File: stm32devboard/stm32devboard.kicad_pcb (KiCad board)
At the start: 4 copper layers, 20.3 x 61 mm, 44 parts, among them J1 Conn_01x20, J2 Conn_01x20, J3 USB_C_Receptacle_USB2.0, J4 ARM_SWD_TagConnect_TC2030-NL, SW1 SW_SPST, SW2 SW_SPST, U1 STM32F042C6Tx, U2 AP63203WU, U3 TCAN332, U4 IP4234CZ6,125, X1 ECS-160-10-36Q-ES-TR

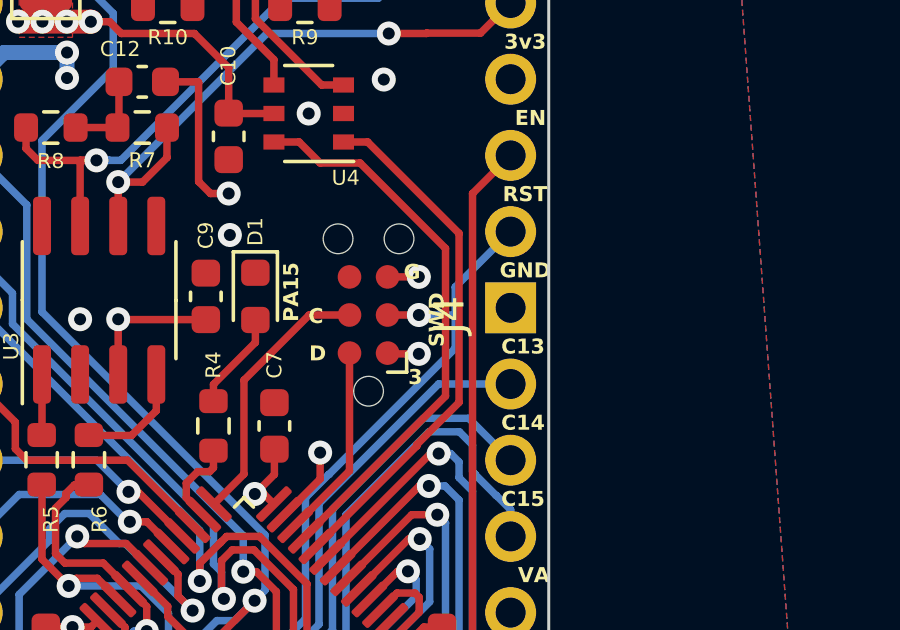
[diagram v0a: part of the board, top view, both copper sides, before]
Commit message: Added title silkscreen
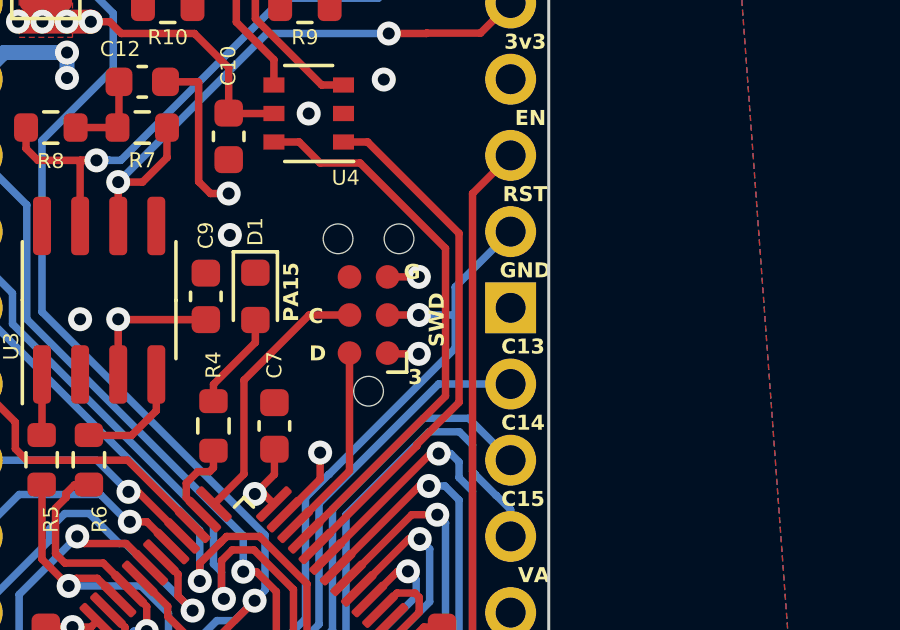
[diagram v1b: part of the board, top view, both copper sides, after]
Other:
- board text added: "STM32F042C6T Dev board ${REVISION} ${ISSUE_DATE} Benjamin Crall"
- board text added: "https://github.com /psas/mints- scada-hardware"
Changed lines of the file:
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@@
 	)
 	(paper "A4")
+	(title_block
+		(title "STM32F042C6T Dev Board")
+		(date "2024-03-11")
+		(rev "v1.0")
+		(company "PSAS / Benjamin Crall")
+	)
 	(layers
 		(0 "F.Cu" signal)
@@
 			(outputformat 1)
 			(mirror no)
-			(drillshape 1)
+			(drillshape 0)
 			(scaleselection 1)
-			(outputdirectory "")
+			(outputdirectory "pcb")
 		)
 	)
@@
 			(at 0 2.7 -90)
 			(layer "F.SilkS")
+			(hide yes)
 			(effects
 				(font
@@
 		(layer "Edge.Cuts")
 	)
+	(gr_text "STM32F042C6T\nDev board ${REVISION}\n${ISSUE_DATE}\nBenjamin Crall\n"
+		(at 148 77.77 0)
+		(layer "B.SilkS")
+		(effects
+			(font
+				(size 1 1)
+				(thickness 0.15)
+			)
+			(justify bottom mirror)
+		)
+	)
+	(gr_text "https://github.com\n/psas/mints-\nscada-hardware"
+		(at 148.08 128.4 0)
+		(layer "B.SilkS")
+		(effects
+			(font
+				(size 1 1)
+				(thickness 0.15)
+			)
+			(justify bottom mirror)
+		)
+	)
 	(gr_text "PB9-TX"

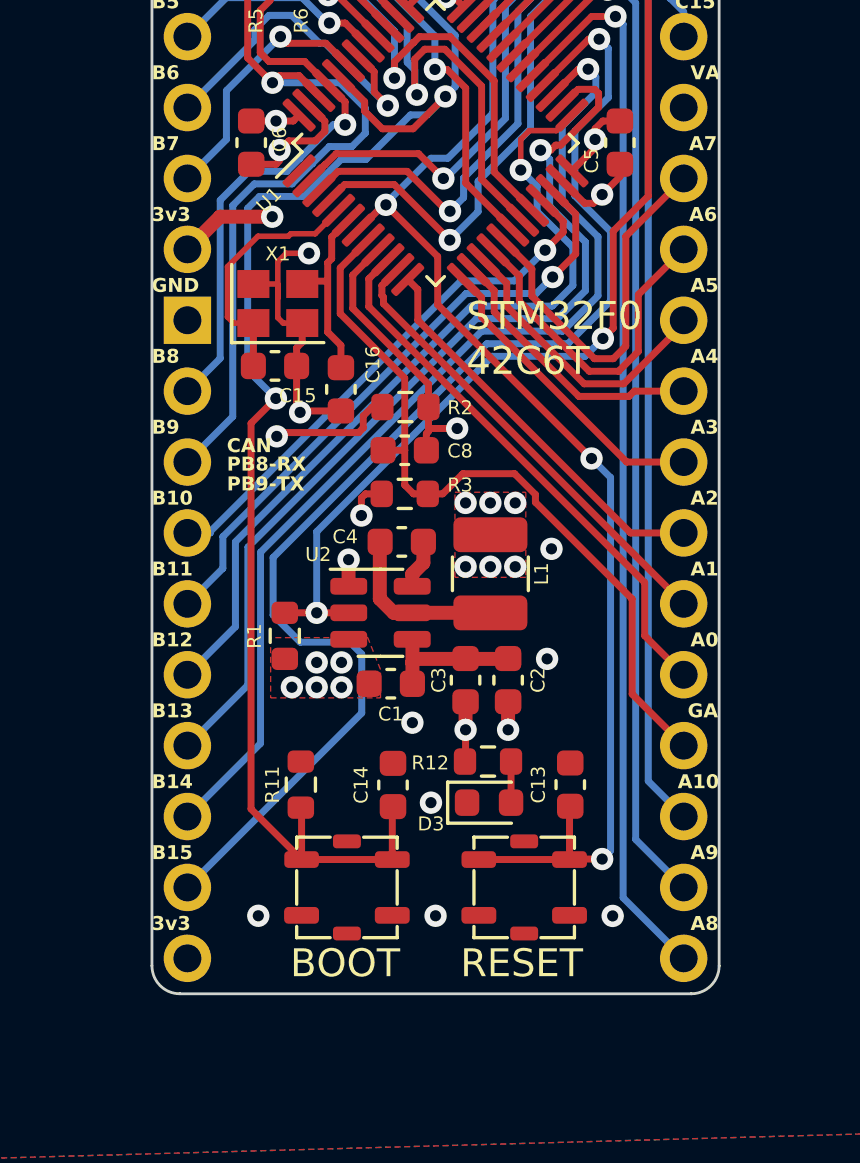
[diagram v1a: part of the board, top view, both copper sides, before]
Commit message: Fixed boot button and updated silkscreen
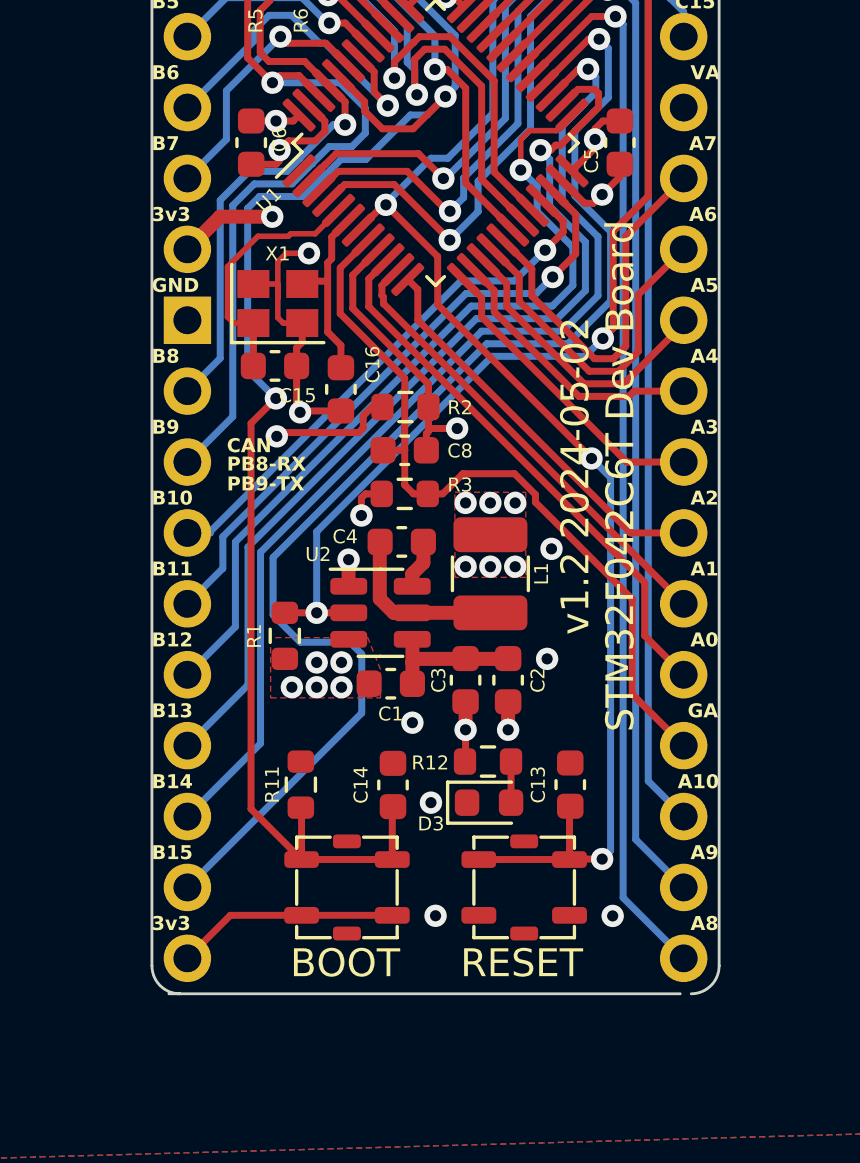
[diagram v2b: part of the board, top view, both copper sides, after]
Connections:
- SW2 pad 2: GND -> +3V3
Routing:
- net +3V3: track 43.6 -> 51.6 mm
- net GND: vias 24 -> 23
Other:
- outline, holes or cut-outs redrawn
- board text added: "${REVISION} ${ISSUE_DATE} ${TITLE}"
- board text added: "https://github.com/psas/mints-scada-hardware"
- board text removed: "STM32F0 42C6T"
- board text removed: "STM32F042C6T Dev board ${REVISION} ${ISSUE_DATE} Benjamin Crall"
- board text removed: "https://github.com /psas/mints- scada-hardware"
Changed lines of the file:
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@@
 	(title_block
 		(title "STM32F042C6T Dev Board")
-		(date "2024-03-11")
-		(rev "v1.0")
+		(date "2024-05-02")
+		(rev "v1.2")
 		(company "PSAS / Benjamin Crall")
 	)
@@
 			(layers "F.Cu" "F.Paste" "F.Mask")
 			(roundrect_rratio 0.25)
-			(net 40 "GND")
+			(net 42 "+3V3")
 			(pinfunction "B")
 			(pintype "passive")
@@
 			(layers "F.Cu" "F.Paste" "F.Mask")
 			(roundrect_rratio 0.25)
-			(net 40 "GND")
+			(net 42 "+3V3")
 			(pinfunction "B")
 			(pintype "passive")
@@
 	)
 	(gr_line
-		(start 157.253807 131.053)
-		(end 138.933807 131.053)
+		(start 156.86 131.053)
+		(end 138.54 131.053)
 		(stroke
 			(width 0.1)
@@
 		(layer "Edge.Cuts")
 	)
-	(gr_text "STM32F042C6T\nDev board ${REVISION}\n${ISSUE_DATE}\nBenjamin Crall\n"
-		(at 148 77.77 0)
-		(layer "B.SilkS")
-		(effects
-			(font
-				(size 1 1)
-				(thickness 0.15)
-			)
-			(justify bottom mirror)
-		)
-	)
-	(gr_text "https://github.com\n/psas/mints-\nscada-hardware"
-		(at 148.08 128.4 0)
+	(gr_text "https://github.com/psas/mints-scada-hardware"
+		(at 149.2 92.7 -90)
 		(layer "B.SilkS")
 		(effects
@@
 		)
 	)
-	(gr_text "STM32F0\n42C6T"
-		(at 149.1996 108.966 0)
-		(layer "F.SilkS")
-		(effects
-			(font
-				(size 1 1)
-				(thickness 0.15)
-			)
-			(justify left bottom)
-		)
-	)
 	(gr_text "B10"
 		(at 137.922 113.5888 0)
@@
 		)
 	)
+	(gr_text "${REVISION} ${ISSUE_DATE}\n${TITLE}"
+		(at 155.3 112.5 90)
+		(layer "F.SilkS")
+		(effects
+			(font
+				(size 1 1)
+				(thickness 0.15)
+			)
+			(justify bottom)
+		)
+	)
 	(gr_text "A2"
 		(at 157.226 113.5888 0)
@@
 	)
 	(via
-		(at 141.743807 128.259)
-		(size 0.8)
-		(drill 0.4)
-		(layers "F.Cu" "B.Cu")
-		(free yes)
-		(net 40)
-	)
-	(via
 		(at 151.293807 78.248)
 		(size 0.5)
@@
 	)
 	(segment
+		(start 146.543807 128.243)
+		(end 140.743807 128.243)
+		(width 0.25)
+		(layer "F.Cu")
+		(net 42)
+	)
+	(segment
 		(start 142.378807 99.785)
 		(end 142.995143 99.785)
@@
 		(width 0.25)
 		(layer "F.Cu")
+		(net 42)
+	)
+	(segment
+		(start 140.743807 128.243)
+		(end 139.203807 129.783)
+		(width 0.25)
+		(layer "F.Cu")

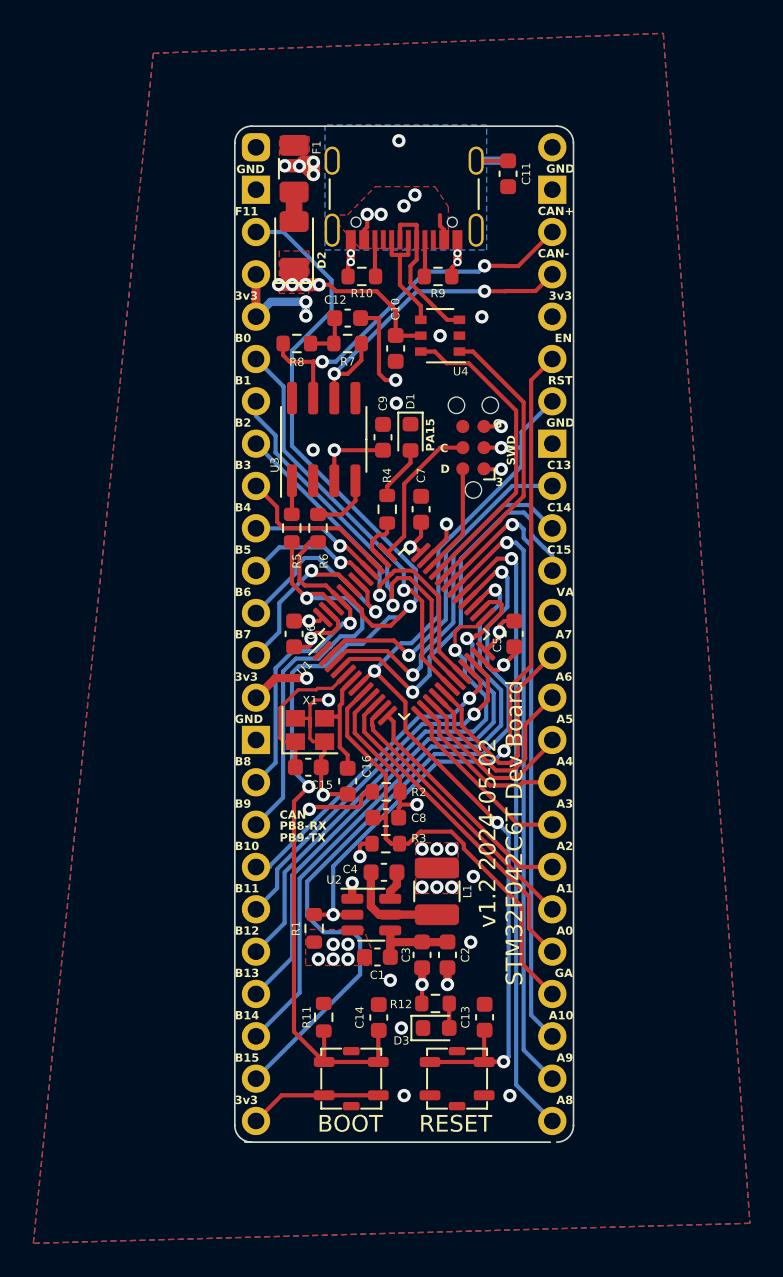
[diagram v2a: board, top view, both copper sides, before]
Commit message: Exported devboard STEP
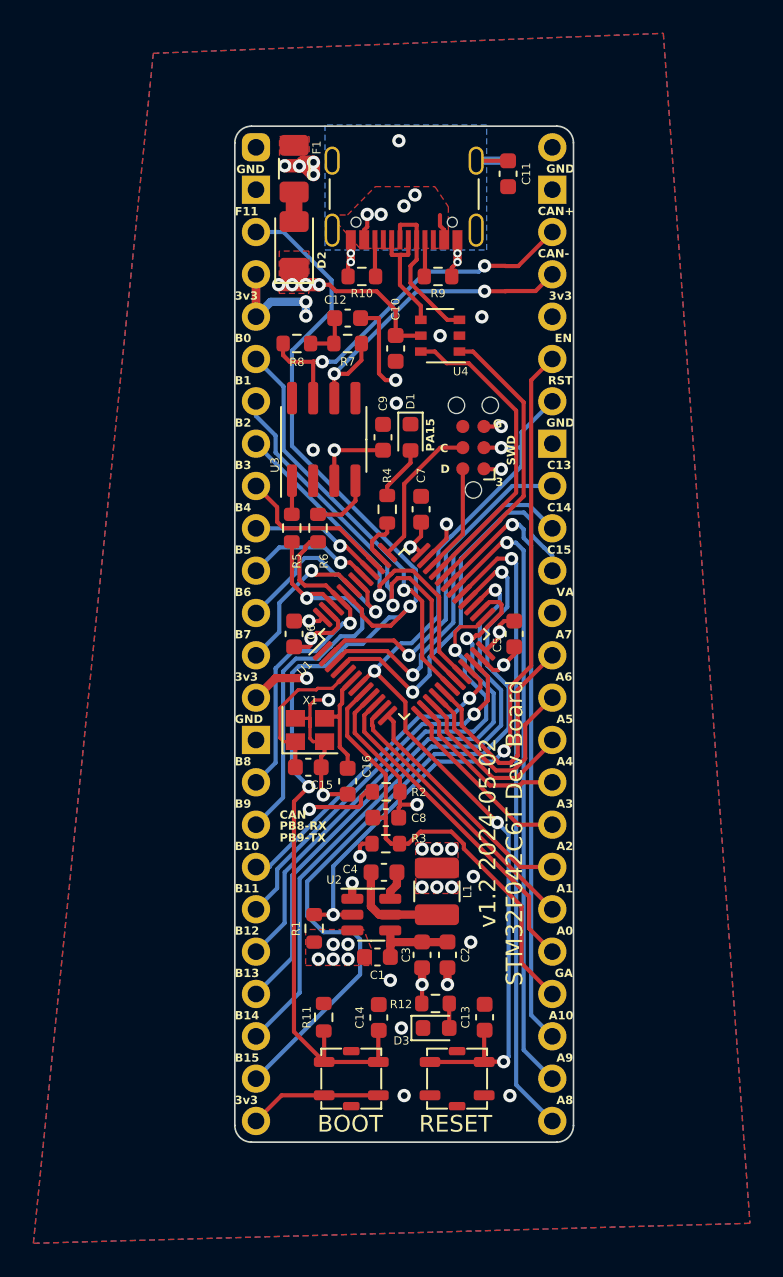
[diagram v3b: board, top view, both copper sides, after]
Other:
- outline, holes or cut-outs redrawn
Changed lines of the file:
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@@
 	)
 	(gr_line
-		(start 156.86 131.053)
-		(end 138.54 131.053)
+		(start 157.25 131.053)
+		(end 138.925 131.053)
 		(stroke
 			(width 0.1)
@@
 	(gr_line
 		(start 138.933807 70.093)
-		(end 157.253807 70.093)
+		(end 157.25 70.093)
 		(stroke
 			(width 0.1)
